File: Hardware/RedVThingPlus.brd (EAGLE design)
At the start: 68.6 x 53.3 mm, 138 parts, among them J1 FEMALE 2x3, J2 USB Female Type C Connector, J5 JTAG, Q1 3.1A/30V/105mΩ, U1 MCP73831, U2 1.8V, U3 AP2112-3.3V, U4 FE310, U5 32MB, Y1 32.768KHZ, Y2 16MHz

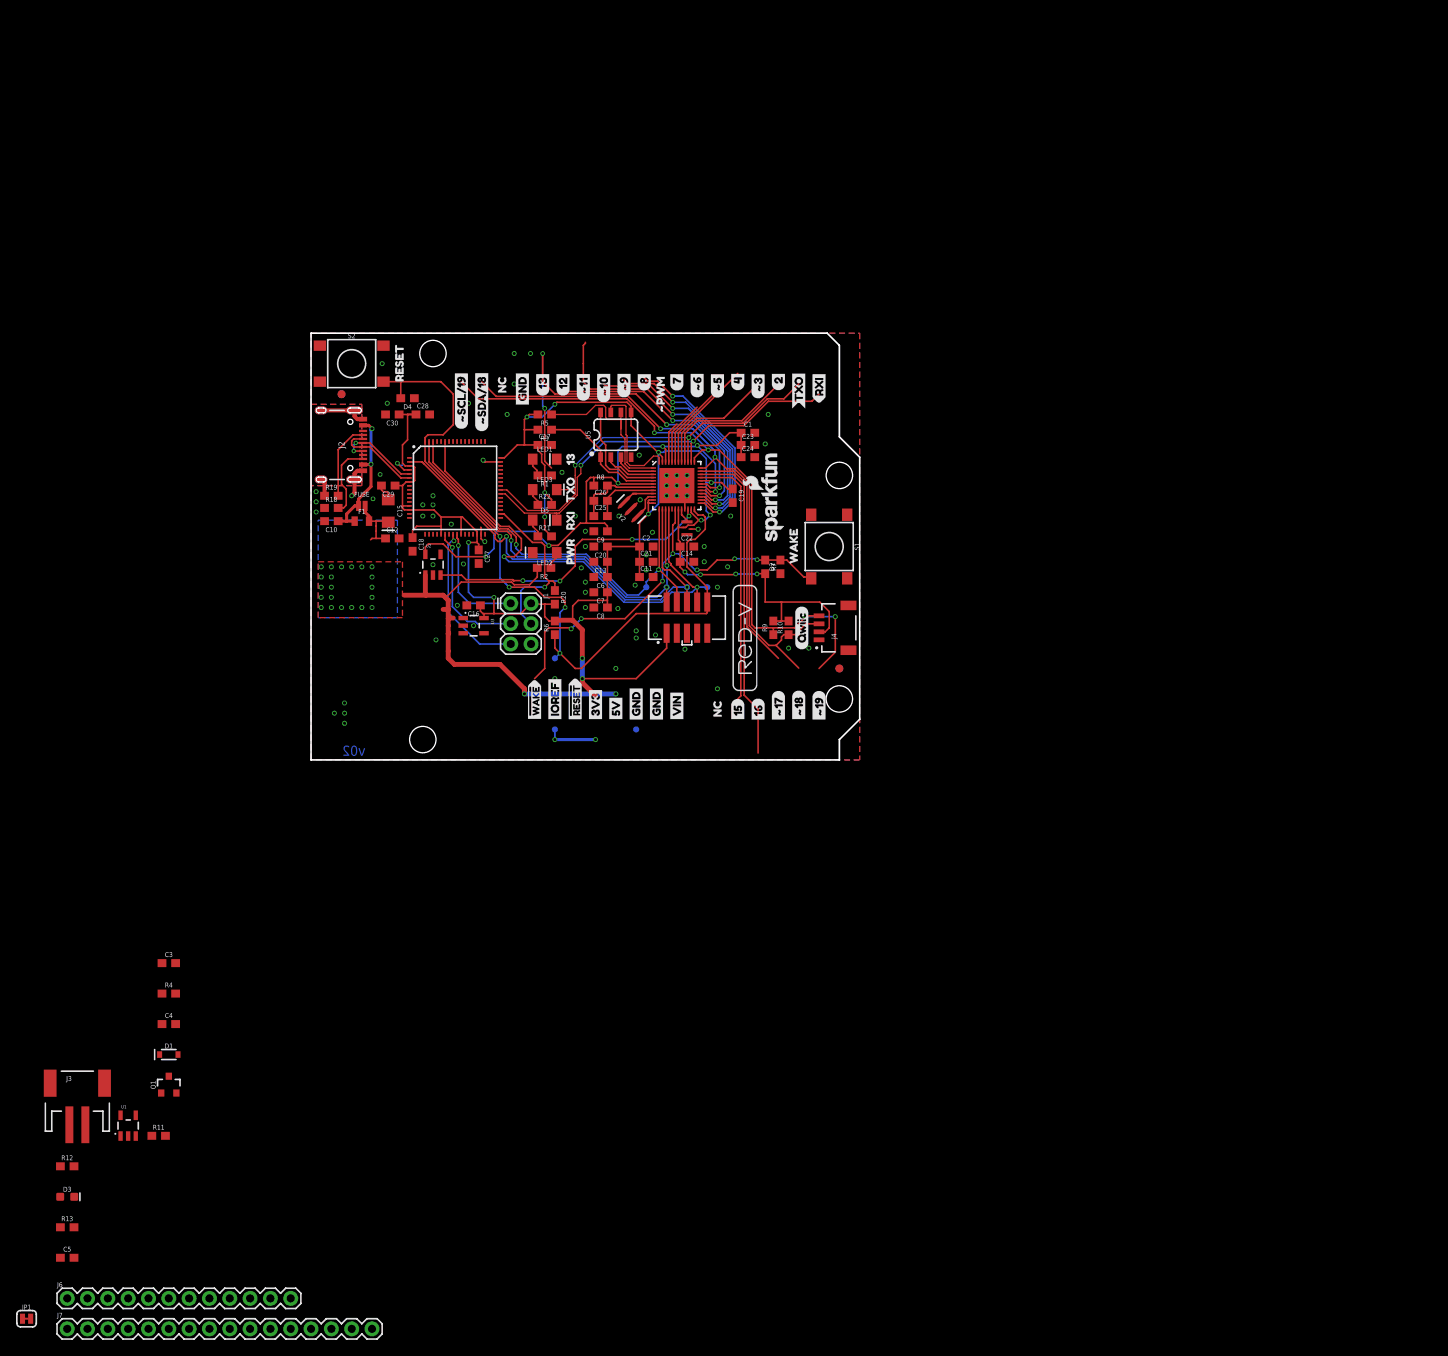
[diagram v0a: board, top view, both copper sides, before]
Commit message: all components placed, midway through routing
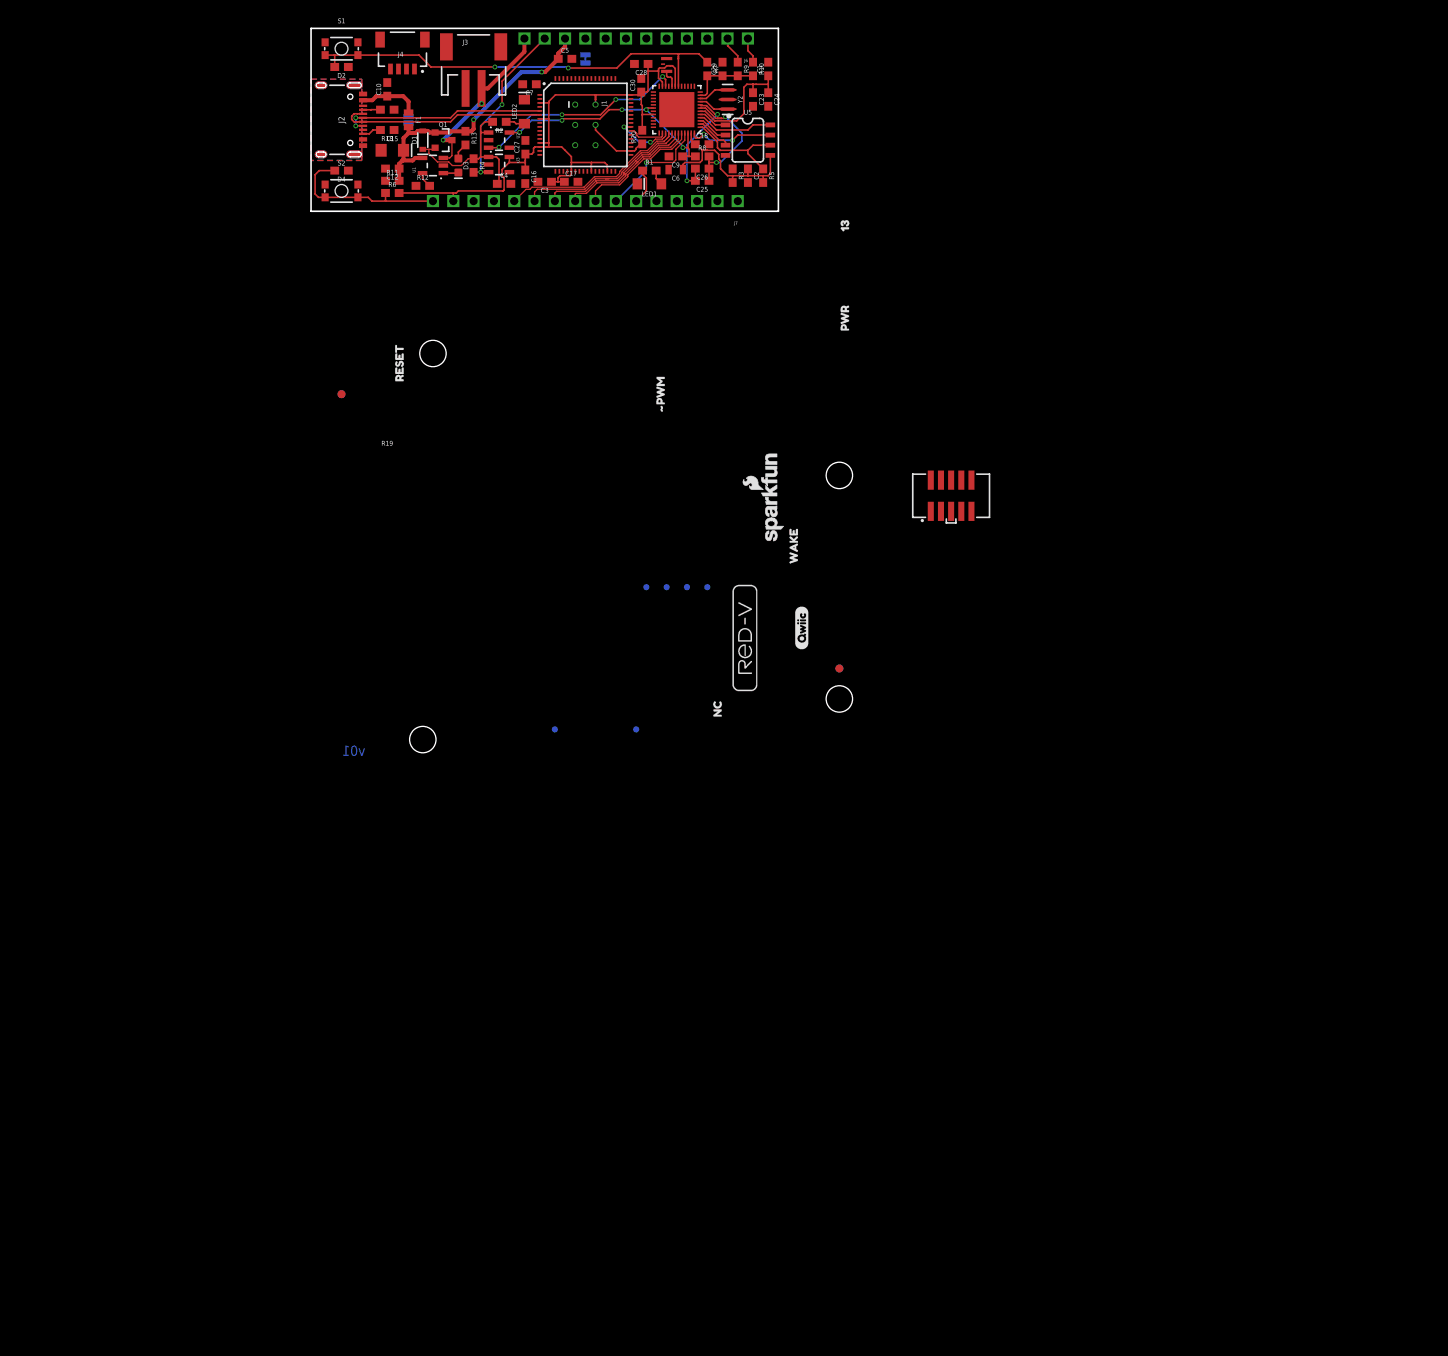
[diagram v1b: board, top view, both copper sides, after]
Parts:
- removed C11, C13, C8: 10uF, SparkFun-Capacitors:0603
- removed C14, C19, C20, C21, C22: 0.1uF, SparkFun-Capacitors:0603
- removed D5: YELLOW, SparkFun-LED:LED-1206-HIDDENSILK
- removed LED3: GREEN, SparkFun-LED:LED-1206
- removed R21, R22: 4.7k, SparkFun-Resistors:0603
- removed TP5: TEST-POINT3, SparkFun-Connectors:PAD.03X.03
- removed U$14: (no value), buzzard_labels (6):#1017
- removed U$15: (no value), buzzard_labels (6):#1116
- removed U$17: (no value), buzzard_labels (6):#1710
- removed U$18: (no value), buzzard_labels (6):#1812
- removed U$19: (no value), buzzard_labels (6):#1911
- removed U$2: (no value), buzzard_labels (6):#324
- removed U$20: (no value), buzzard_labels (6):#RESET2
- removed U$21: (no value), buzzard_labels (6):#SCL#1926
- removed U$22: (no value), buzzard_labels (6):#SDA#1827
- removed U$23: (no value), buzzard_labels (6):#WAKE0
- removed U$24: (no value), buzzard_labels (6):3V33
- removed U$25: (no value), buzzard_labels (6):5V4
- removed U$26: (no value), buzzard_labels (6):158
- removed U$27: (no value), buzzard_labels (6):169
- removed U$28: (no value), buzzard_labels (6):225
- removed U$29: (no value), buzzard_labels (6):423
- removed U$3: (no value), buzzard_labels (6):#522
- removed U$30: (no value), buzzard_labels (6):720
- removed U$31: (no value), buzzard_labels (6):819
- removed U$32: (no value), buzzard_labels (6):1215
- removed U$33: (no value), buzzard_labels (6):1314
- removed U$34, U$35, U$36: (no value), buzzard_labels (6):GND5
- removed U$37: (no value), buzzard_labels (6):IOREF1
- removed U$39: (no value), buzzard_labels (6):RXI29
- removed U$4: (no value), buzzard_labels (6):#621
- removed U$40: (no value), buzzard_labels (6):TXO28
- removed U$41: (no value), buzzard_labels (6):VIN6
- removed U$43: (no value), buzzard_labels (6):NC7
- removed U$47: (no value), buzzard_labels (7):RXI1
- removed U$48: (no value), buzzard_labels (7):TXO2
- removed U$51: (no value), Redfive_logo#07#png (1):REDFIVE_LOGO#07#PNG
- removed U$9: (no value), buzzard_labels (6):#918
- C6: value 10uF -> 47uF/6.3V; device SparkFun-Capacitors:0603 -> SparkFun-Capacitors:0805
- C7: value 10uF -> 470nF
- J1: device SparkFun-Connectors:2X3 -> SparkFun-Connectors:2X3_TEST_POINTS
- J6: device SparkFun-Connectors:1X12 -> SparkFun-Connectors:1X12_SM_SQ_NOSILK
- J7: device SparkFun-Connectors:1X16 -> SparkFun-Connectors:1X16_SM_SQ_NOSILK
- S1, S2: value MOMENTARY-SWITCH-SPST-SMD-6.2MM-TALL -> MOMENTARY-SWITCH-SPST-SMD-4.6X2.8MM; device SparkFun-Switches:TACTILE_SWITCH_SMD_6.2MM_TALL -> SparkFun-Switches:TACTILE_SWITCH_SMD_4.6X2.8MM
- moved J6 179.0 mm to (54.6, 90.2), turned to 180 degrees
- moved JP1 172.3 mm to (34.3, 87.6), flipped to the bottom, turned to 90 degrees
- moved J7 164.0 mm to (53.3, 69.8), turned to 180 degrees
- moved C5 162.3 mm to (31.8, 87.6)
- moved R13 145.0 mm to (19.3, 77.7), turned to 270 degrees
- moved J3 138.7 mm to (20.3, 87.6)
- moved D3 137.9 mm to (18.4, 74.3), turned to 270 degrees
- moved R12 130.4 mm to (14.0, 71.8)
- moved U1 125.9 mm to (15.2, 74.3), turned to 90 degrees
- moved Q1 123.0 mm to (16.5, 77.5), turned to 270 degrees
- moved R11 122.9 mm to (10.2, 72.4)
- moved D1 118.6 mm to (14.0, 77.5), turned to 90 degrees
- moved C4 113.1 mm to (24.1, 72.0)
- moved R4 110.3 mm to (20.3, 74.3), turned to 270 degrees
- moved C3 108.4 mm to (29.2, 72.3), turned to 180 degrees
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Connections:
- removed net N$13: D5.A, R21.1
- removed net N$6: LED3.A, R22.1
- net !RESET: now also S2.1, S2.2; no longer S2.A2, TP5.P$1
- net !WAKE: now also S1.1, S1.2; no longer S1.A2
- net 3.3V: no longer C11.1, C13.1, C14.1, C19.1, C20.1, C21.1, C22.1, C8.1, R21.2, R22.2
- net GND: now also S1.3, S1.4, S2.3, S2.4; no longer C11.2, C13.2, C14.2, C19.2, C20.2, C21.2, C22.2, C8.2, S1.B2, S2.B2
- net RXI: no longer D5.C
- net TXO: no longer LED3.C
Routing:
- net 3.3V: track 251.2 -> 116.8 mm, vias 19 -> 0
- net SCL: track 83.8 -> 3.49 mm, vias 4 -> 0
- net !RESET: track 98.8 -> 21.2 mm, vias 4 -> 0
- net SDA: track 74.9 -> 3.22 mm, vias 2 -> 0
- net TDI: track 62.6 -> 0.00 mm, vias 2 -> 0
- net TDO: track 57.8 -> 0.00 mm, vias 2 -> 0
- net TCK: track 52.9 -> 0.00 mm, vias 2 -> 0
- net TMS: track 52.6 -> 0.00 mm, vias 3 -> 0
- net RXI: track 52.5 -> 5.08 mm, vias 2 -> 0
- net SPI_SCK: track 51.3 -> 4.53 mm, vias 4 -> 0
- net TXO: track 52.6 -> 7.55 mm
- net IO10: track 40.2 -> 0.00 mm
- net SPI_MOSI: track 36.2 -> 0.00 mm, vias 2 -> 0
- net IO9: track 32.3 -> 0.00 mm
- net 5V: track 54.0 -> 21.8 mm, vias 23 -> 0
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- removed copper zone on layer 1, net 5V
- removed copper zone on layer 16, net 5V
- removed copper zone on layer 1, net GND
- removed copper zone on layer 16, net GND
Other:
- board size 68.6 x 53.3 mm -> 58.4 x 22.9 mm
- board text added: "v01"
- board text removed: "v02"

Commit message: initial layout complete, needs silk
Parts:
- removed J5: JTAG, SparkFun-Connectors:2X5-SMD-1.27MM
- removed TP1, TP2, TP3, TP4, TP6, TP7: TEST-POINT3, SparkFun-Connectors:PAD.03X.03
- moved JP15 74.2 mm to (76.2, 62.2)
- moved JP16 74.2 mm to (138.4, 27.9)
- moved JP3 74.2 mm to (86.4, 19.1)
- moved JP4 74.2 mm to (138.4, 24.1)
- moved JP5 74.2 mm to (138.4, 52.1)
- moved JP6 74.2 mm to (87.6, 67.3)
- moved JP8 74.2 mm to (138.4, 27.9)
- moved JP9 74.2 mm to (76.2, 62.2)
- moved LOGO1 74.2 mm to (130.0, 49.4)
- moved U$16 74.2 mm to (74.9, 64.8)
- moved U$38 74.2 mm to (123.2, 21.0)
- moved U$42 74.2 mm to (116.1, 58.7)
- moved U$46 74.2 mm to (139.1, 69.2)
- moved U$50 74.2 mm to (132.7, 40.1)
- moved U$52 74.2 mm to (126.6, 31.8)
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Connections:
- net !RESET: no longer J5.10
- net 3.3V: no longer J5.1, TP6.P$1
- net GND: no longer J5.3, J5.5, J5.9, TP7.P$1
- net TCK: no longer J5.4, TP2.P$1
- net TDI: no longer J5.8, TP4.P$1
- net TDO: no longer J5.6, TP3.P$1
- net TMS: no longer J5.2, TP1.P$1
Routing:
- net SDA: track 3.22 -> 70.3 mm, vias 0 -> 4
- net SCL: track 3.49 -> 67.7 mm, vias 0 -> 2
- net !RESET: track 21.2 -> 61.9 mm, vias 0 -> 3
- net 3.3V: track 116.8 -> 154.9 mm
- net TDO: track 0.00 -> 22.4 mm, vias 0 -> 2
- net TCK: track 0.00 -> 21.7 mm, vias 0 -> 2
- net TMS: track 0.00 -> 20.9 mm, vias 0 -> 2
- net IO2: track 0.00 -> 19.4 mm, vias 0 -> 1
- net TDI: track 0.00 -> 19.2 mm, vias 0 -> 2
- net TXO: track 7.55 -> 26.6 mm
- net IO9: track 0.00 -> 17.9 mm, vias 0 -> 1
- net SPI_MISO: track 0.00 -> 17.4 mm, vias 0 -> 1
- net SPI_MOSI: track 0.00 -> 17.3 mm, vias 0 -> 1
- net IO10: track 0.00 -> 16.5 mm, vias 0 -> 1
- net IO11: track 0.00 -> 15.9 mm, vias 0 -> 1
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- added copper zone on layer 1, net GND
- added copper zone on layer 16, net GND

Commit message: v10 changes for Reds design review
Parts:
- removed JP1: JUMPER-SMT_2_NC_TRACE_SILK, SparkFun-Jumpers:SMT-JUMPER_2_NC_TRACE_SILK
- removed JP3, JP4, JP5, JP6: STAND-OFF, SparkFun:STAND-OFF
- added I2C: JUMPER-SMT_3_NO_NO-SILK, SparkFun-Jumpers:SMT-JUMPER_3_NO_NO-SILK
- added NC/GND: JUMPER-SMT_2_NO_NO-SILK, SparkFun-Jumpers:SMT-JUMPER_2_NO_NO-SILK
- added U$11: (no value), buzzard_labels (1):118
- added U$12: (no value), buzzard_labels (1):1811
- added U$14: (no value), buzzard_labels (1):1912
- added U$15: (no value), buzzard_labels (1):2013
- added U$17: (no value), buzzard_labels (1):2114
- added U$18: (no value), buzzard_labels (1):2215
- added U$19: (no value), buzzard_labels (1):2316
- added U$2: (no value), buzzard_labels (1):96
- added U$20: (no value), buzzard_labels (1):EN18
- added U$21, U$28: (no value), buzzard_labels (1):GND0
- added U$22, U$27: (no value), buzzard_labels (1):NC17
- added U$23: (no value), buzzard_labels (1):RXI2
- added U$24: (no value), buzzard_labels (1):SCK5
- added U$25: (no value), buzzard_labels (1):SCL10
- added U$26: (no value), buzzard_labels (1):VBAT19
- added U$29: (no value), buzzard_labels (2):#RESET34
- added U$3: (no value), buzzard_labels (2):26
- added U$30: (no value), buzzard_labels (2):3V332
- added U$31: (no value), buzzard_labels (2):3V333
- added U$32: (no value), buzzard_labels (2):015
- added U$33: (no value), buzzard_labels (2):114
- added U$34: (no value), buzzard_labels (2):213
- added U$35: (no value), buzzard_labels (2):912
- added U$36: (no value), buzzard_labels (2):1011
- added U$37: (no value), buzzard_labels (2):1110
- added U$39: (no value), buzzard_labels (2):1828
- added U$4: (no value), buzzard_labels (2):15
- added U$40: (no value), buzzard_labels (2):1927
- added U$41: (no value), buzzard_labels (2):2026
- added U$43: (no value), buzzard_labels (2):2125
- added U$47: (no value), buzzard_labels (2):2323
- added U$48: (no value), buzzard_labels (2):EN8
- added U$5: (no value), buzzard_labels (2):04
- added U$51, U$67: (no value), buzzard_labels (2):GND29
- added U$53: (no value), buzzard_labels (2):MOSI#320
- added U$54: (no value), buzzard_labels (2):NC#GND31
- added U$55: (no value), buzzard_labels (2):NC30
- added U$56: (no value), buzzard_labels (2):RST2
- added U$57: (no value), buzzard_labels (2):RXI#1619
- added U$58: (no value), buzzard_labels (2):SCK#522
- added U$59: (no value), buzzard_labels (2):SCL#1316
- added U$6: (no value), buzzard_labels (1):SDA9
- added U$60: (no value), buzzard_labels (2):SDA#1217
- added U$61: (no value), buzzard_labels (2):SI0
- added U$62: (no value), buzzard_labels (2):SO1
- added U$63: (no value), buzzard_labels (2):TXO#1718
- added U$64: (no value), buzzard_labels (2):VBAT7
- added U$65: (no value), buzzard_labels (2):VUSB3
- added U$66: (no value), buzzard_labels (2):VUSB9
- added U$68: (no value), buzzard_labels (3):RESET1
- added U$69: (no value), buzzard_labels (3):WAKE0
- added U$8: (no value), buzzard_labels (1):TXO1
- added U$9: (no value), buzzard_labels (1):107
- added U6: FE310, SparkFun-IC-Microcontroller:QFN-48-.4MMPITCH
- J4: value (none) -> QWIIC_RIGHT_ANGLE
- U$38: device buzzard_labels (6):NC7 -> buzzard_labels (4):CHG0
- U$42: device buzzard_labels (6):_#PWM30 -> Redfive_logo#04#jpg (3):REDFIVE_LOGO#04#JPG
- U$44: value MK22FN128VLH10 -> (none); device SparkFun-IC-Comms:LQFP-64 -> buzzard_labels (2):2224
- U$45: device buzzard_labels (7):133 -> seggerlogo#png:SEGGERLOGO#PNG
- U$46: device buzzard_labels (7):PWR0 -> buzzard_labels (5):51
- U$49: device buzzard_labels (8):RESET0 -> buzzard_labels (6):THING_PLUS0
- U$50: device buzzard_labels (8):WAKE1 -> buzzard_labels (8):I2C_______0
- U$52: device Redfive_logo#05#png (2):REDFIVE_LOGO#05#PNG -> buzzard_labels (2):MISO#421
- U2: value 1.8V -> AP2127K-1.8V
- U4: value FE310 -> MK22FN128VLH10; device SparkFun-IC-Microcontroller:QFN-48-.4MMPITCH -> SparkFun-IC-Comms:LQFP-64
- U5: value 32MB -> 32MBit
- moved JP16 133.1 mm to (7.24, 5.71)
- moved JP8 133.1 mm to (7.24, 5.71)
- moved U$1 125.9 mm to (8.64, 16.0), turned to 0 degrees
- moved U$46 120.5 mm to (38.2, 3.30), turned to 0 degrees
- moved LOGO1 112.2 mm to (24.5, 11.4), flipped to the bottom
- moved U$38 108.1 mm to (16.5, 3.56), turned to 0 degrees
- moved U$42 105.6 mm to (21.6, 11.6), flipped to the bottom
- moved U$16 90.5 mm to (1.83, 11.4), turned to 90 degrees
- moved U$49 85.3 mm to (19.0, 7.00), flipped to the bottom
- moved U$52 85.2 mm to (47.0, 1.52), flipped to the bottom
- moved U$50 80.3 mm to (57.1, 13.0), flipped to the bottom
- moved U$45 74.5 mm to (10.5, 16.3), flipped to the bottom
- moved JP15 44.9 mm to (57.1, 21.6)
- moved JP9 44.9 mm to (57.1, 21.6)
- moved U4 12.2 mm to (34.3, 10.8), turned to 0 degrees
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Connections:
- new net N$5: I2C.1, R9.2
- new net N$6: I2C.3, R10.2
- net !RESET: now also U4.64, U6.24; no longer U$44.64, U4.24
- net !WAKE: now also U6.18; no longer U4.18
- net 1.8V: now also U6.30, U6.46, U6.6; no longer U4.30, U4.46, U4.6
- net 3.3V: now also I2C.2, U4.13, U4.14, U4.21, U4.26, U4.3, U4.30, U4.48, U4.7, U5.8, U6.11, U6.12, U6.19, U6.23, U6.32, U6.47; no longer R10.2, R9.2, U$44.13, U$44.14, U$44.21, U$44.26, U$44.3, U$44.30, U$44.48, U$44.7, U4.11, U4.12, U4.19, U4.23, U4.32, U4.47, U5.5
- net CORE_ENABLE: now also U6.22; no longer U4.22
- net D+: now also U4.5; no longer U$44.5
- net D-: now also U4.6; no longer U$44.6
- net DBG_RESET: now also U4.34; no longer U$44.34
- net DBG_SWDCLK: now also U4.22; no longer U$44.22
- net DBG_SWDIO: now also U4.25; no longer U$44.25
- net DBG_SWO: now also U4.24; no longer U$44.24
- net GND: now also NC/GND.1, U4.15, U4.16, U4.31, U4.4, U4.47, U6.21, U6.49; no longer J2.SHLD1, J2.SHLD2, J2.SHLD3, J2.SHLD4, J2.SHLD5, J2.SHLD6, J2.SHLD7, J2.SHLD8, JP1.1, U$44.15, U$44.16, U$44.31, U$44.4, U$44.47, U4.21, U4.49
- net IO0: now also U6.25; no longer U4.25
- net IO1: now also U6.26; no longer U4.26
- net IO10: now also U6.34; no longer U4.34
- net IO11: now also U6.35; no longer U4.35
- net IO18: now also U6.40; no longer U4.40
- net IO19: now also U6.41; no longer U4.41
- net IO2: now also U6.27; no longer U4.27
- net IO20: now also U6.42; no longer U4.42
- net IO21: now also U6.43; no longer U4.43
- net IO22: now also U6.44; no longer U4.44
- net IO23: now also U6.45; no longer U4.45
- net IO9: now also U6.33; no longer U4.33
- net N$10: now also U6.8; no longer U4.8
- net N$3: now also U6.10; no longer U4.10
- net N$4: now also NC/GND.2; no longer JP1.2
- net N$7: now also U6.9; no longer U4.9
- net N$8: now also U6.20; no longer U4.20
- net PLL_AVDD: now also U6.7; no longer U4.7
- net QSPI_0: now also U5.5, U6.4; no longer U4.4, U5.8
- net QSPI_1: now also U6.3; no longer U4.3
- net QSPI_2: now also U6.2; no longer U4.2
- net QSPI_3: now also U5.7, U6.1; no longer U4.1, U5.6
- net QSPI_CS: now also U6.5; no longer U4.5
- net QSPI_SCK: now also U5.6, U6.48; no longer U4.48, U5.7
- net RXI: now also U4.40, U6.38; no longer U$44.39, U4.38
- net SCL: now also U6.37; no longer U4.37
- net SDA: now also U6.36; no longer U4.36
- net SPI_MISO: now also U6.29; no longer U4.29
- net SPI_MOSI: now also U6.28; no longer U4.28
- net SPI_SCK: now also U6.31; no longer U4.31
- net TCK: now also U4.62, U6.13; no longer U$44.62, U4.13
- net TDI: now also U4.59, U6.16; no longer U$44.59, U4.16
- net TDO: now also U4.2, U6.14; no longer U$44.2, U4.14
- net TMS: now also U4.63, U6.15; no longer U$44.63, U4.15
- net TXO: now also U6.39; no longer U$44.40
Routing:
- net 3.3V: track 154.9 -> 174.4 mm, vias 0 -> 7
- net N$6: track 0.00 -> 4.91 mm, vias 0 -> 1
- net N$5: track 0.00 -> 4.59 mm, vias 0 -> 1
- net QSPI_0: track 9.03 -> 12.0 mm, vias 0 -> 2
- net RXI: track 19.2 -> 21.4 mm
- net GND: track 2.38 -> 4.61 mm, vias 37 -> 50
- net DBG_RESET: track 8.00 -> 10.2 mm
- net QSPI_SCK: track 9.65 -> 11.3 mm, vias 2 -> 4
- net IO21: track 18.0 -> 16.7 mm
- net N$4: track 2.03 -> 0.86 mm
- net IO19: track 22.5 -> 21.4 mm
- net DBG_SWDIO: track 8.97 -> 10.0 mm
- net IO22: track 16.1 -> 15.2 mm
- net !RESET: track 61.9 -> 62.8 mm
- net IO20: track 20.3 -> 19.5 mm
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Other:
- board text added: "v10"
- board text removed: "Based on Arduino by: M. Banzi, D. Cuartielles, T. Igoe, G. Martino, D. Mellis"
- board text removed: "v01"

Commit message: post review changes
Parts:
- added LOGO2: SFE_LOGO_FLAME.2_INCH, SparkFun-Aesthetics:SFE_LOGO_FLAME_.2
- LED1: value Blue -> BLUE; device SparkFun-LED:LED-1206-HIDDENSILK -> SparkFun-LED:LED-0603
- U$46: device buzzard_labels (5):51 -> buzzard_labels (9):50
- moved R1 0.74 mm to (41.9, 4.45)
- moved U$46 0.51 mm to (38.7, 3.30)
- moved LED1 0.46 mm to (41.9, 3.05)
- moved U$51 0.22 mm to (24.1, 1.30)
- moved NC/GND 0.19 mm to (34.3, 20.1)
- moved U$3 0.06 mm to (43.4, 20.1)
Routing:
- net SPI_SCK: track 17.6 -> 16.3 mm
- net N$1: track 2.05 -> 1.41 mm
- net GND: vias 50 -> 52
